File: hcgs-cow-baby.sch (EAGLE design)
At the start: 27 parts, among them SW3 MIDI PWR, T1 2N3904

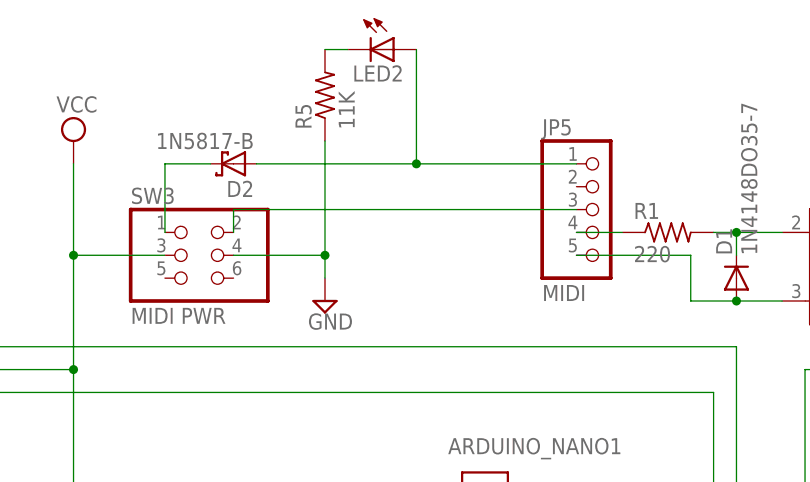
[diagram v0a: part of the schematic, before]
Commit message: fixed schematic for power thru pins
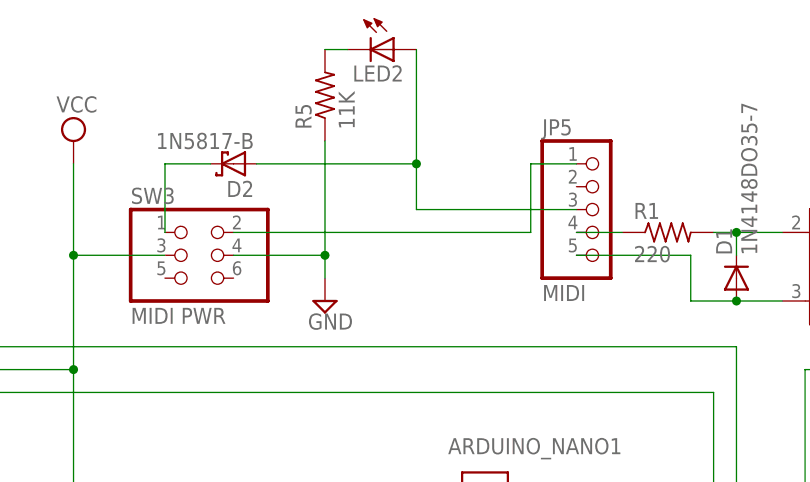
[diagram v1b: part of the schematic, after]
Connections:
- removed net N$9: JP5.3, SW3.2
- new net N$24: JP5.1, SW3.2
- net N$6: now also JP5.3; no longer JP5.1
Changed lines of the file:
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@@
 <net name="N$6" class="0">
 <segment>
-<pinref part="JP5" gate="A" pin="1"/>
 <pinref part="D2" gate="G$1" pin="A"/>
-<wire x1="119.38" y1="96.52" x2="101.6" y2="96.52" width="0.1524" layer="91"/>
 <pinref part="LED2" gate="G$1" pin="A"/>
 <wire x1="101.6" y1="96.52" x2="83.82" y2="96.52" width="0.1524" layer="91"/>
 <wire x1="101.6" y1="109.22" x2="101.6" y2="96.52" width="0.1524" layer="91"/>
+<pinref part="JP5" gate="A" pin="3"/>
+<wire x1="119.38" y1="91.44" x2="101.6" y2="91.44" width="0.1524" layer="91"/>
+<wire x1="101.6" y1="91.44" x2="101.6" y2="96.52" width="0.1524" layer="91"/>
 <junction x="101.6" y="96.52"/>
 </segment>
@@
 <pinref part="SW3" gate="A" pin="1"/>
 <wire x1="73.66" y1="96.52" x2="73.66" y2="88.9" width="0.1524" layer="91"/>
-</segment>
-</net>
-<net name="N$9" class="0">
-<segment>
-<pinref part="JP5" gate="A" pin="3"/>
-<wire x1="119.38" y1="91.44" x2="81.28" y2="91.44" width="0.1524" layer="91"/>
-<pinref part="SW3" gate="A" pin="2"/>
-<wire x1="81.28" y1="91.44" x2="81.28" y2="88.9" width="0.1524" layer="91"/>
 </segment>
 </net>
@@
 </segment>
 </net>
+<net name="N$24" class="0">
+<segment>
+<pinref part="JP5" gate="A" pin="1"/>
+<wire x1="119.38" y1="96.52" x2="114.3" y2="96.52" width="0.1524" layer="91"/>
+<wire x1="114.3" y1="96.52" x2="114.3" y2="88.9" width="0.1524" layer="91"/>
+<pinref part="SW3" gate="A" pin="2"/>
+<wire x1="114.3" y1="88.9" x2="81.28" y2="88.9" width="0.1524" layer="91"/>
+</segment>
+</net>
